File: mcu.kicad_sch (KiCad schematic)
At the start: 58 parts, among them P20 HEADER-2x11, P22 HEADER-2x13, P26 LPC_JTAG, P28 HEADER-2x11, SW1 SWITCH, SW2 SWITCH, U20 W25Q16, U23 LPC4330FET180, X2 MCU_XTAL, X3 RTC_XTAL

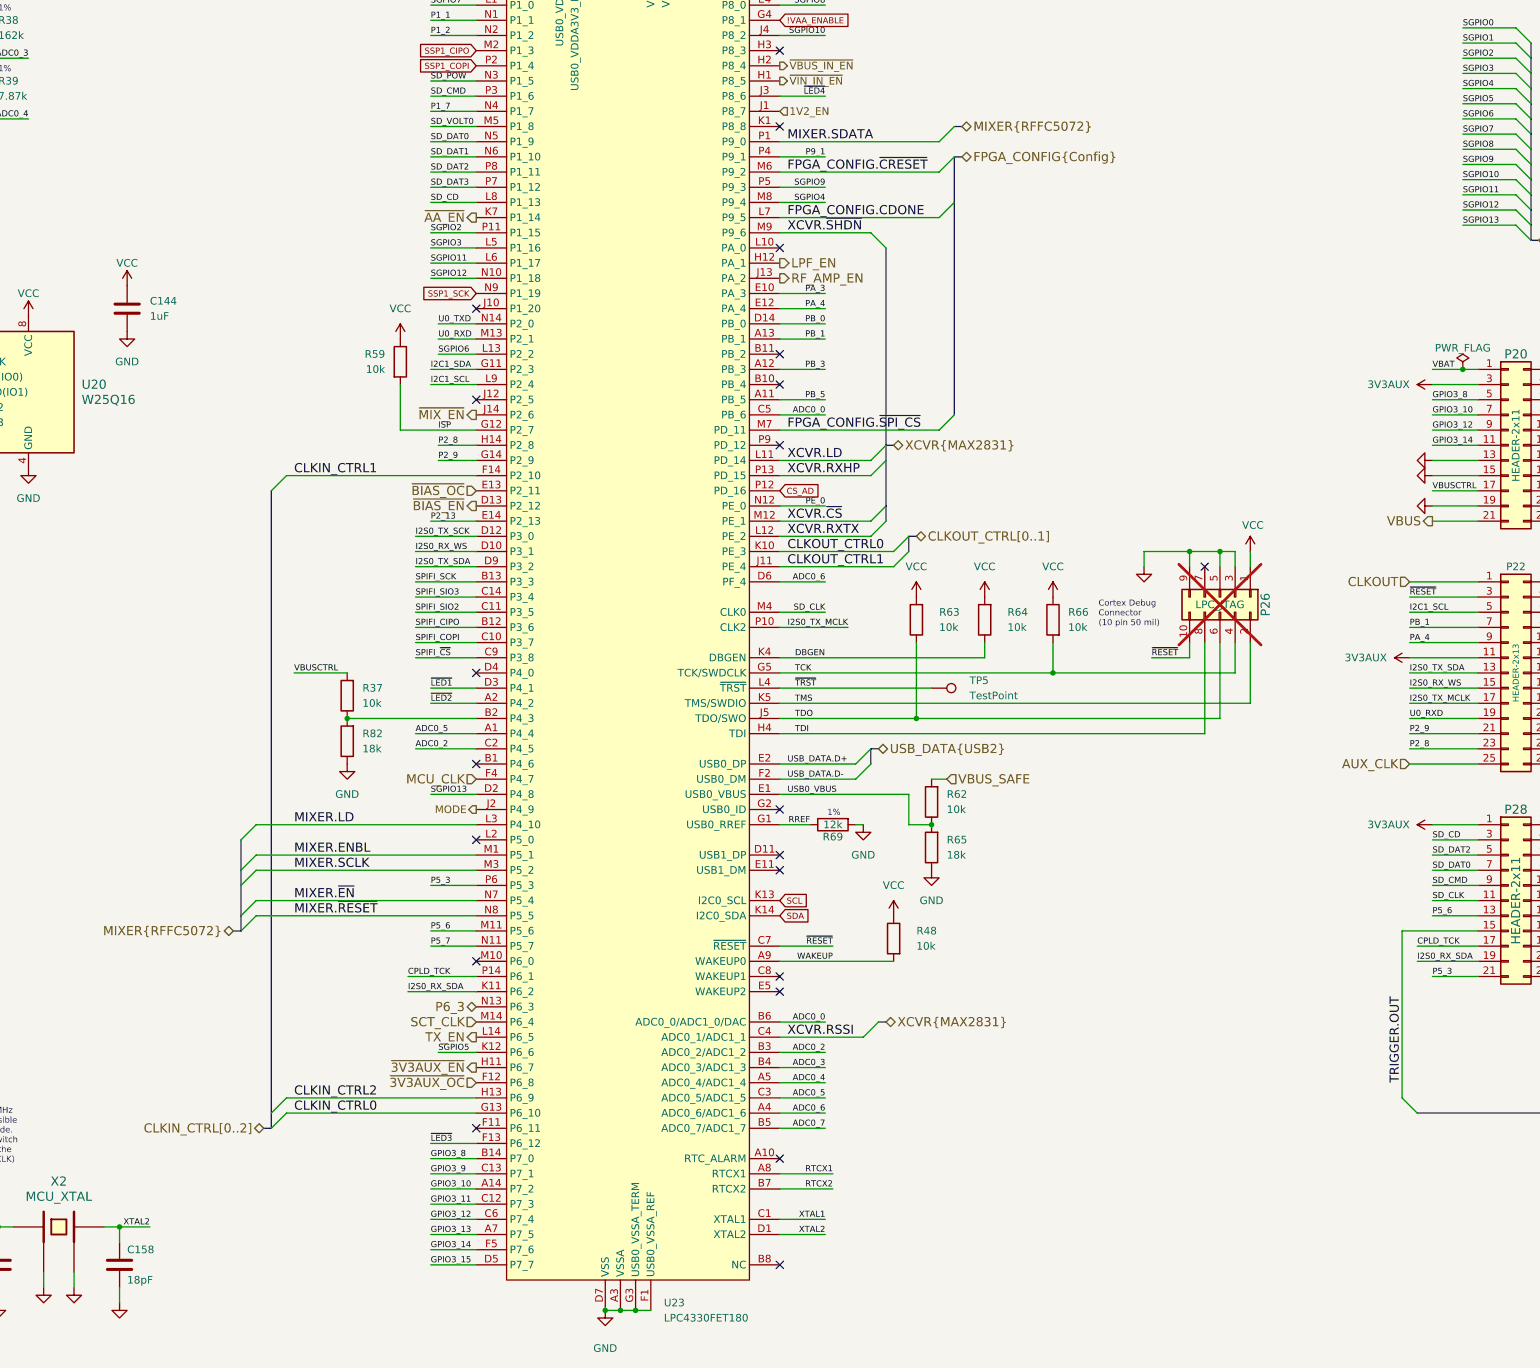
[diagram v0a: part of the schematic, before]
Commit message: Remove GND zone from front layer F.Cu
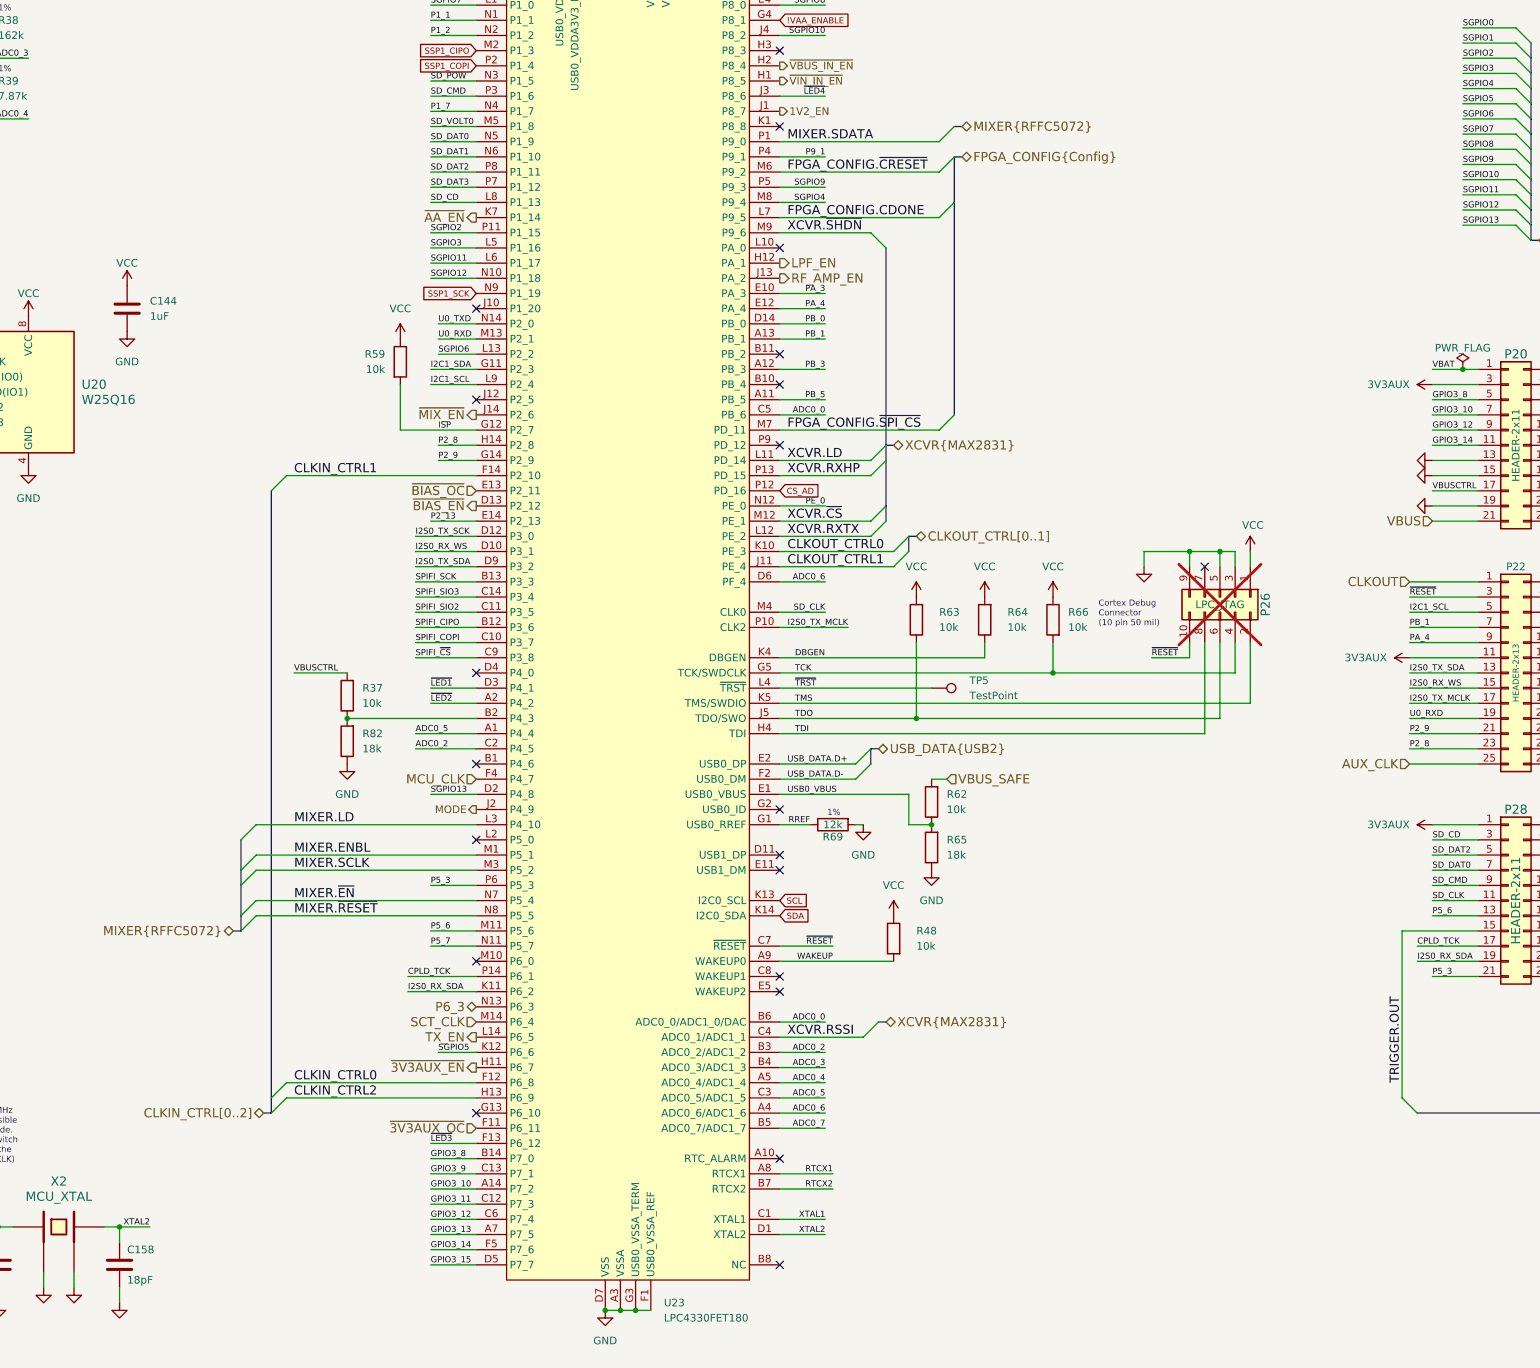
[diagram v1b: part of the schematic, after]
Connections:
- net CLKIN_CTRL0: now also U23.F12 (P6_8); no longer U23.G13 (P6_10)
- net ~{3V3AUX_OC}: now also U23.F11 (P6_11); no longer U23.F12 (P6_8)
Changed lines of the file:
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@@
 	)
 	(no_connect
-		(at 245.11 185.42)
+		(at 194.31 226.06)
 	)
 	(no_connect
-		(at 245.11 205.74)
+		(at 245.11 185.42)
 	)
 	(no_connect
-		(at 194.31 228.6)
+		(at 245.11 205.74)
 	)
 	(no_connect
@@
 	)
 	(bus_entry
-		(at 160.02 228.6)
+		(at 160.02 223.52)
 		(size 2.54 -2.54)
 		(stroke
@@
 	(bus
 		(pts
-			(xy 160.02 121.92) (xy 160.02 226.06)
+			(xy 160.02 121.92) (xy 160.02 223.52)
 		)
 		(stroke
@@
 		)
 	)
-	(bus
-		(pts
-			(xy 160.02 226.06) (xy 160.02 228.6)
-		)
-		(stroke
-			(width 0)
-			(type default)
-		)
-	)
 	(wire
 		(pts
@@
 	(bus
 		(pts
-			(xy 158.75 228.6) (xy 160.02 228.6)
+			(xy 158.75 226.06) (xy 160.02 226.06)
 		)
 		(stroke
@@
 	(wire
 		(pts
-			(xy 162.56 226.06) (xy 194.31 226.06)
+			(xy 162.56 220.98) (xy 194.31 220.98)
 		)
 		(stroke
@@
 		)
 	)
+	(bus
+		(pts
+			(xy 160.02 223.52) (xy 160.02 226.06)
+		)
+		(stroke
+			(width 0)
+			(type default)
+		)
+	)
 	(wire
 		(pts
@@
 	)
 	(label "CLKIN_CTRL0"
-		(at 163.83 226.06 0)
+		(at 163.83 220.98 0)
 		(effects
 			(font
@@
 	)
 	(hierarchical_label "VBUS"
-		(shape output)
+		(shape input)
 		(at 354.33 127 180)
 		(effects
@@
 	)
 	(hierarchical_label "1V2_EN"
-		(shape input)
+		(shape output)
 		(at 245.11 58.42 0)
 		(effects
@@
 	(hierarchical_label "CLKIN_CTRL[0..2]"
 		(shape bidirectional)
-		(at 158.75 228.6 180)
+		(at 158.75 226.06 180)
 		(effects
 			(font
@@
 	(hierarchical_label "~{3V3AUX_OC}"
 		(shape input)
-		(at 194.31 220.98 180)
+		(at 194.31 228.6 180)
 		(effects
 			(font
@@
 		)
 		(property "Value" "GND"
-			(at 215.9 265.43 0)
+			(at 215.9 264.16 0)
 			(effects
 				(font
